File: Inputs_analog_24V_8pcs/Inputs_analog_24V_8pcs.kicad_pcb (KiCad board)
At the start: 2 copper layers, 146.1 x 101.6 mm, 102 parts, among them J1 Screw_Terminal_01x02, J10 Screw_Terminal_01x03, J11 Screw_Terminal_01x03, J2 Screw_Terminal_01x02, J3 Screw_Terminal_01x06, J4 Screw_Terminal_01x03, J5 Screw_Terminal_01x03, J6 Screw_Terminal_01x03, J7 Screw_Terminal_01x03, J8 Screw_Terminal_01x03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

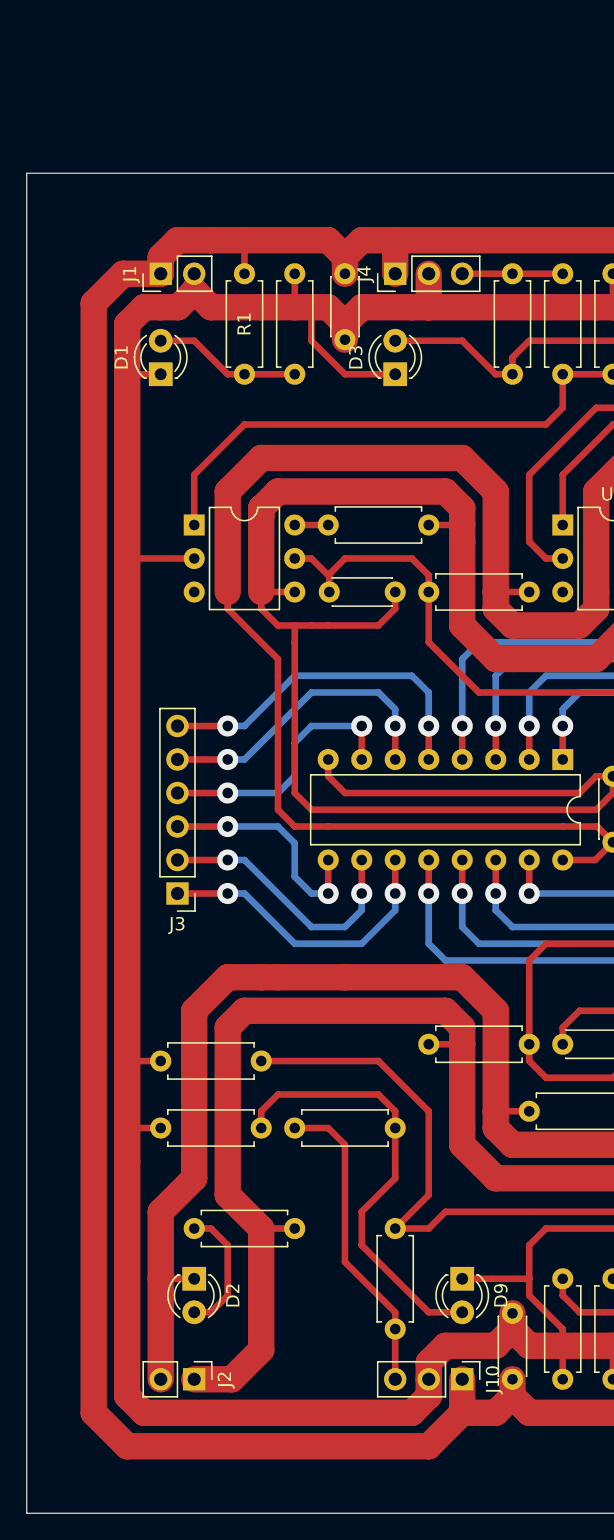
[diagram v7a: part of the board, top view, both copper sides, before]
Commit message: Change footprints for ternimals
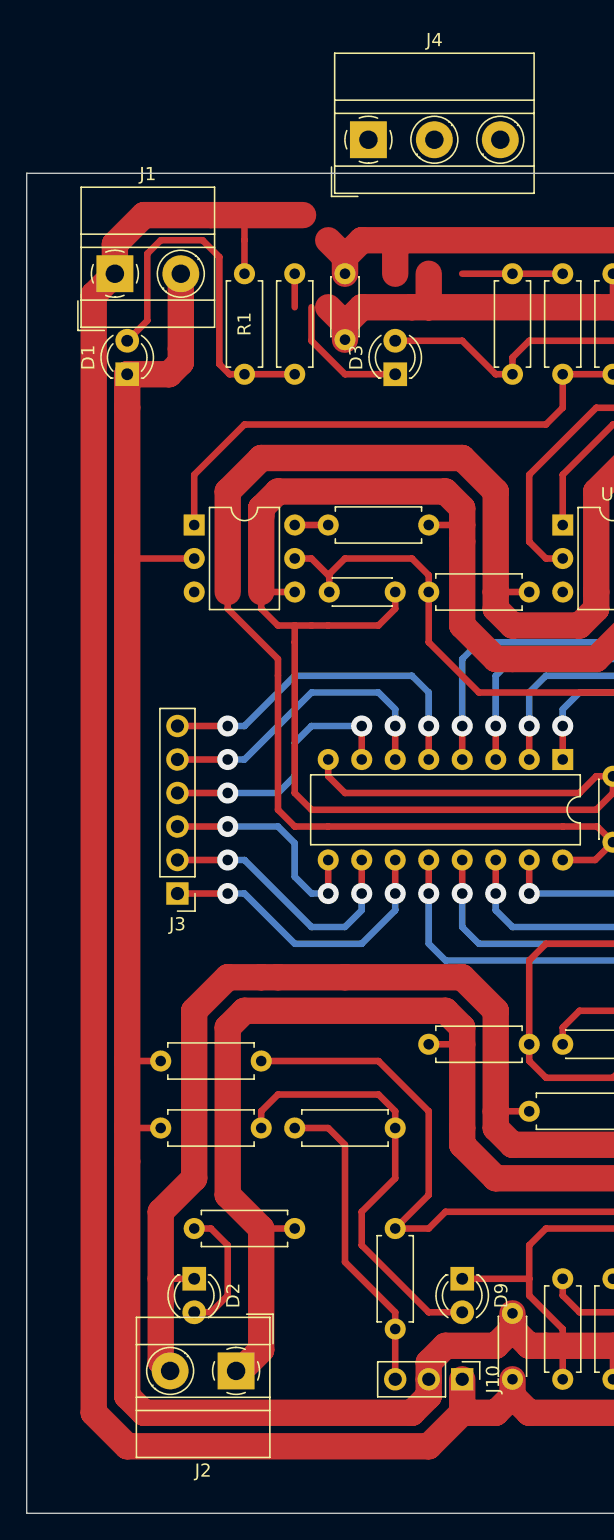
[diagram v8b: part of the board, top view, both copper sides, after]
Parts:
- J1, J2: footprint Connector_PinHeader_2.54mm:PinHeader_1x02_P2.54mm_Vertical -> TerminalBlock_MetzConnect:TerminalBlock_MetzConnect_Type011_RT05502HBWC_1x02_P5.00mm_Horizontal
- J4: footprint Connector_PinHeader_2.54mm:PinHeader_1x03_P2.54mm_Vertical -> TerminalBlock_MetzConnect:TerminalBlock_MetzConnect_Type011_RT05503HBWC_1x03_P5.00mm_Horizontal
- moved J4 10.4 mm to (53.8, 30.5), turned to 0 degrees
- moved J1 3.48 mm to (34.6, 40.6), turned to 0 degrees
- moved J2 3.24 mm to (43.8, 123.8), turned to 180 degrees
- moved D1 2.54 mm to (35.6, 48.3)
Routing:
- net Net-(D1-Pad2): track 11.2 -> 27.8 mm
- net Earth: track 731.4 -> 718.1 mm
- net +5V: track 675.4 -> 671.9 mm
- net +24V: track 351.4 -> 353.7 mm
